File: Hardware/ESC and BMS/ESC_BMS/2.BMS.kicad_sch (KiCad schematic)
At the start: 0 parts

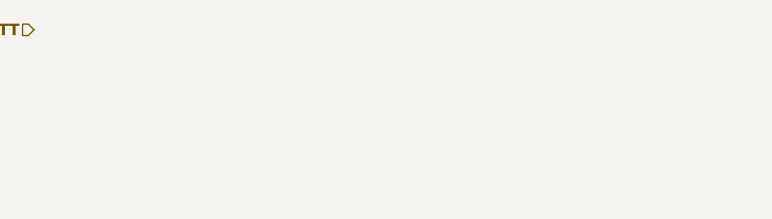
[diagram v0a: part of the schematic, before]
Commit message: Updated 2.BMS.kicad_sch to add bulk capacitance
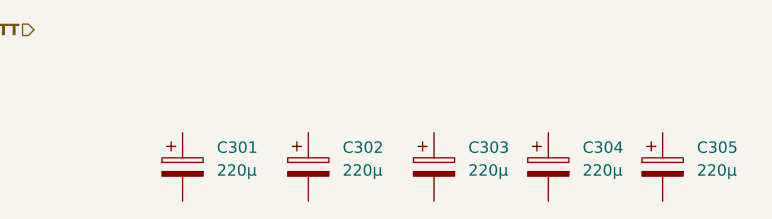
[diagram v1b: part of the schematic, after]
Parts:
- added C301, C302, C303, C304, C305: 220µ, Capacitor_SMD:CP_Elec_6.3x5.9, symbol Device:C_Polarized

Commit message: initial BMS work
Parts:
- added U12: BQ2969T, symbol ESC_BMS:BQ2969T
- renumbered C301 to C21, C302 to C22, C303 to C23, C304 to C24, C305 to C25
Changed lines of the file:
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@@
 		(dnp no)
 		(fields_autoplaced yes)
-		(property "Reference" "C301"
+		(property "Reference" "C21"
 			(at 48.26 35.9409 0)
 			(effects
@@
 			(project ""
 				(path "/64aee9f2-a448-43ef-b28d-f00e276bd9f5/eb2740b7-11f5-4644-9e72-e71a449b99af"
-					(reference "C301")
+					(reference "C21")
+					(unit 1)
+				)
+			)
+		)
+	)
+	(symbol
+		(lib_id "ESC_BMS:BQ2969T")
+		(at 95.25 54.61 0)
+		(unit 1)
+		(exclude_from_sim no)
+		(in_bom yes)
+		(on_board yes)
+		(dnp no)
+		(fields_autoplaced yes)
+		(property "Reference" "U12"
+			(at 97.79 46.99 0)
+			(effects
+				(font
+					(size 1.27 1.27)
+				)
+			)
+		)
+		(property "Value" "BQ2969T"
+			(at 97.79 49.53 0)
+			(effects
+				(font
+					(size 1.27 1.27)
+				)
+			)
+		)
+		(property "Footprint" ""
+			(at 95.25 54.61 0)
+			(effects
+				(font
+					(size 1.27 1.27)
+				)
+				(hide yes)
+			)
+		)
+		(property "Datasheet" "https://www.ti.com/lit/ds/symlink/bq2962.pdf?ts=1761657217789&ref_url=https%253A%252F%252Fwww.ti.com%252Fproduct%252FBQ2962"
+			(at 97.282 72.644 0)
+			(effects
+				(font
+					(size 1.27 1.27)
+				)
+				(hide yes)
+			)
+		)
+		(property "Description" "BQ296xxx Overvoltage Protection for 2-Series, 3-Series, and 4-Series Cell Li-Ion Batteries with Regulated Output Supply"
+			(at 98.298 76.2 0)
+			(effects
+				(font
+					(size 1.27 1.27)
+				)
+				(hide yes)
+			)
+		)
+		(pin "3"
+		)
+		(pin "4"
+		)
+		(pin "2"
+		)
+		(pin "9"
+		)
+		(pin "8"
+		)
+		(pin "7"
+		)
+		(pin "6"
+		)
+		(pin "1"
+		)
+		(pin "5"
+		)
+		(instances
+			(project ""
+				(path "/64aee9f2-a448-43ef-b28d-f00e276bd9f5/eb2740b7-11f5-4644-9e72-e71a449b99af"
+					(reference "U12")
 					(unit 1)
 				)
@@
 		(dnp no)
 		(fields_autoplaced yes)
-		(property "Reference" "C305"
+		(property "Reference" "C25"
 			(at 101.6 35.9409 0)
 			(effects
@@
 			(project "SPROJ3EE_ESC_BMS"
 				(path "/64aee9f2-a448-43ef-b28d-f00e276bd9f5/eb2740b7-11f5-4644-9e72-e71a449b99af"
-					(reference "C305")
+					(reference "C25")
 					(unit 1)
 				)
@@
 		(dnp no)
 		(fields_autoplaced yes)
-		(property "Reference" "C303"
+		(property "Reference" "C23"
 			(at 76.2 35.9409 0)
 			(effects
@@
 			(project "SPROJ3EE_ESC_BMS"
 				(path "/64aee9f2-a448-43ef-b28d-f00e276bd9f5/eb2740b7-11f5-4644-9e72-e71a449b99af"
-					(reference "C303")
+					(reference "C23")
 					(unit 1)
 				)
@@
 		(dnp no)
 		(fields_autoplaced yes)
-		(property "Reference" "C304"
+		(property "Reference" "C24"
 			(at 88.9 35.9409 0)
 			(effects
@@
 			(project "SPROJ3EE_ESC_BMS"
 				(path "/64aee9f2-a448-43ef-b28d-f00e276bd9f5/eb2740b7-11f5-4644-9e72-e71a449b99af"
-					(reference "C304")
+					(reference "C24")
 					(unit 1)
 				)
@@
 		(dnp no)
 		(fields_autoplaced yes)
-		(property "Reference" "C302"
+		(property "Reference" "C22"
 			(at 62.23 35.9409 0)
 			(effects
@@
 			(project "SPROJ3EE_ESC_BMS"
 				(path "/64aee9f2-a448-43ef-b28d-f00e276bd9f5/eb2740b7-11f5-4644-9e72-e71a449b99af"
-					(reference "C302")
-					(unit 1)
-				)
+					(reference "C22")
+					(unit 1)
+				)

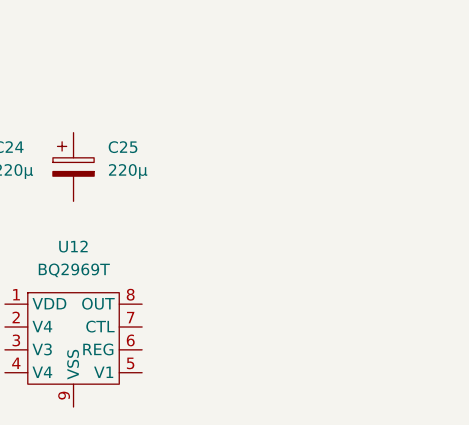
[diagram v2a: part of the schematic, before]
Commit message: some more BMS work + fixed RP2040 XIN/XOUT shortage
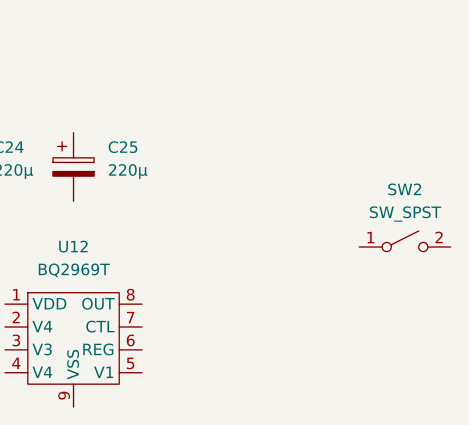
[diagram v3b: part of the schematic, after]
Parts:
- added SW2: SW_SPST, symbol Switch:SW_SPST
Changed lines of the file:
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@@
+	)
+	(symbol
+		(lib_id "Switch:SW_SPST")
+		(at 134.62 46.99 0)
+		(unit 1)
+		(exclude_from_sim no)
+		(in_bom yes)
+		(on_board yes)
+		(dnp no)
+		(fields_autoplaced yes)
+		(property "Reference" "SW2"
+			(at 134.62 40.64 0)
+			(effects
+				(font
+					(size 1.27 1.27)
+				)
+			)
+		)
+		(property "Value" "SW_SPST"
+			(at 134.62 43.18 0)
+			(effects
+				(font
+					(size 1.27 1.27)
+				)
+			)
+		)
+		(property "Footprint" ""
+			(at 134.62 46.99 0)
+			(effects
+				(font
+					(size 1.27 1.27)
+				)
+				(hide yes)
+			)
+		)
+		(property "Datasheet" "~"
+			(at 134.62 46.99 0)
+			(effects
+				(font
+					(size 1.27 1.27)
+				)
+				(hide yes)
+			)
+		)
+		(property "Description" "Single Pole Single Throw (SPST) switch"
+			(at 134.62 46.99 0)
+			(effects
+				(font
+					(size 1.27 1.27)
+				)
+				(hide yes)
+			)
+		)
+		(pin "1"
+		)
+		(pin "2"
+		)
+		(instances
+			(project ""
+				(path "/64aee9f2-a448-43ef-b28d-f00e276bd9f5/eb2740b7-11f5-4644-9e72-e71a449b99af"
+					(reference "SW2")
+					(unit 1)
+				)
+			)
+		)
 	)
 	(symbol

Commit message: BMS almost full
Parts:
- added C26, C27, C28, C29, C35, C38: 100n, Capacitor_SMD:C_0603_1608Metric, symbol Device:C
- added C30, C36: 100n, Capacitor_SMD:C_0805_2012Metric_Pad1.18x1.45mm_HandSolder, symbol Device:C
- added C31: 47nF, symbol Device:C_Polarized
- added C32, C33: 1uf, symbol Device:C_Polarized
- added C34: 47uF, symbol Device:C
- added D5, D6: BZX79, Diode_THT:D_DO-35_SOD27_P10.16mm_Horizontal, symbol Diode:ZPDxx
- added D7, D8: LED, symbol Device:LED
- added D9: LED_Dual, symbol Device:LED_Dual_AAKK
- added Q10, Q8: NTD25P03LT4G, symbol Simulation_SPICE:PMOS
- added Q9: NMOS, symbol Simulation_SPICE:NMOS
- added R13, R14: 100k, symbol Device:R
- added R15: 143k, symbol Device:R
- added R16: 1M, symbol Device:R
- added R17: 100, symbol Device:R
- added R18: 0.2, symbol Device:R
- added R19, R20, R21, R22, R24, R25: 1k, symbol Device:R
- added R23: 511, symbol Device:R
- added R26, R27: ?, symbol Device:R
- added TH2: ?, symbol Device:Thermistor_NTC
- added U13: 74AUC2G08, Package_SO:SSOP-8_2.95x2.8mm_P0.65mm, symbol 74xGxx:74AUC2G08
- added U14: TPS25926, Package_SON:VSON-10-1EP_3x3mm_P0.5mm_EP1.65x2.4mm_ThermalVias, symbol Power_Management:TPS2592xx
- added U16: BQ2057, symbol ESC_BMS:BQ2057
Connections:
- net +VBATT: now also SW2.1 (A)
- net VDD: now reaches U12.1 (VDD)
- net VDD: now also C30.1, R17.2
- net at U12.3 (V3): now also C28.1, R19.1
- net at U12.4 (V2): now also C28.2, C29.1, R20.1
- net at U12.5 (V1): now also C29.2, R21.1
- net at U12.6 (REG): now also C34.1
- net at U12.8 (OUT): now also Q9.2 (G)
- net GND: now reaches U12.9 (VSS)
- net GND: now also C26.2, C27.2, C30.2, C31.2, C32.2, C33.2, C34.2, C35.2, C36.1, C36.2, C38.2, D6.1 (K), Q9.3 (S), R14.2, R15.2, R18.1, R22.1, R24.1, R25.1, R26.2, R27.1, TH2.1, U13.4 (GND), U14.11 (GND), U16.3 (VCC), U16.6 (VSS), U16.8 (COMP)
- net at SW2.2 (B): now also Q8.3 (S)
- new net: C32.1, D5.2 (A), Q8.1 (D), R13.2, R16.1, U14.3 (VIN), U14.4 (VIN), U14.5 (VIN)
- new net: C31.1, U14.1 (dV/dT)
- new net: R26.1, R27.2, TH2.2, U16.4 (TS)
- new net: D9.4 (K2), R22.2
- new net: R15.1, U14.10 (ILIM)
- new net: R16.2, U14.2 (EN/UVLO)
- new net: C33.1, Q9.1 (D), R17.1, R19.2, U14.6 (OUT), U14.7 (OUT), U14.8 (OUT)
- new net: D9.2 (A2), D9.3 (K1), R24.2, U16.5 (STAT)
- new net: C38.1, Q10.1 (D), U16.2 (BAT)
- new net: Q10.3 (S), R18.2, U16.1 (SNS)
- new net: D5.1 (K), R14.1
- new net: D9.1 (A1), R23.2
- new net: Q10.2 (G), R25.2, U16.7 (CC)
- new net: D6.2 (A), R23.1
- new net: Q8.2 (G), R13.1
- new net: C35.1, R21.2
- new net VMID: R20.2
- no-connect marks 0 -> 1
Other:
- note added: "BQ2057"
- note added: "BQ2969T"
- note added: "Balancing"
- note added: "Charging"
- note added: "Decoupling caps"
- note added: "FOR Itrip 5A"
- note added: "OCP"
- note added: "RPP"
- note added: "TPS25926"
- moved on the sheet: C21, C22, C23, C24, C25, SW2

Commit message: more BMS
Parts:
- removed C26, C28, C35: 100n, Capacitor_SMD:C_0603_1608Metric, symbol Device:C
- removed C31: 47nF, symbol Device:C_Polarized
- removed C32, C33: 1uf, symbol Device:C_Polarized
- removed D9: LED_Dual, symbol Device:LED_Dual_AAKK
- removed R13: 100k, symbol Device:R
- removed R15: 143k, symbol Device:R
- removed R21: 1k, symbol Device:R
- removed R26, R27: ?, symbol Device:R
- removed TH2: ?, symbol Device:Thermistor_NTC
- removed U13: 74AUC2G08, Package_SO:SSOP-8_2.95x2.8mm_P0.65mm, symbol 74xGxx:74AUC2G08
- removed U14: TPS25926, Package_SON:VSON-10-1EP_3x3mm_P0.5mm_EP1.65x2.4mm_ThermalVias, symbol Power_Management:TPS2592xx
- added C29: 100n, Capacitor_SMD:C_0603_1608Metric, symbol Device:C
- added F2: RUEF Polyfuse, Resistor_THT:R_Axial_DIN0207_L6.3mm_D2.5mm_P10.16mm_Horizontal, symbol Device:Polyfuse
- added Q11: SQJ141ELP, symbol Simulation_SPICE:PMOS
- added R14: 10k, symbol Device:R
- added R25: 1M, symbol Device:R
- C34: value 47uF -> 470nF
- D7: value LED -> KG EELP41.22
- D8: value LED -> LR Q976.01
- Q8: value NTD25P03LT4G -> SQJ141ELP
- R13: renamed from R14; value 100k -> 27k
- R15: renamed from R18; value 0.2 -> ?
- R16: value 1M -> 10k
- renumbered C27 to C21, C30 to C22, C36 to C23, C21 to C24, C22 to C25, C23 to C26, C24 to C27, C25 to C28, C29 to C31, C38 to C32, Q9 to Q10, Q10 to Q9, R23 to R17, R25 to R18, R24 to R19, R19 to R20, R22 to R21, R20 to R22, R17 to R23, U16 to U12, U12 to U13
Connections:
- net GND: now also C24.2, C25.2, C26.2, C27.2, C28.2, R16.1, C29.2, R14.2
- net +VPROT: now reaches C24.1
- net +VPROT: now also C25.1, C26.1, C27.1, C28.1, C32.1, Q9.1 (D), U12.2 (BAT), Q11.3 (S)
- net at U12.4 (TS): now also R16.2, R14.1
- net at R21.2: now also D7.1 (K)
- net at R20.2, R23.1: now also F2.2, Q11.1 (D), R25.1; no longer Q10.1 (D)
- net at Q8.3 (S): now also D5.1 (K), C29.1, F2.1; no longer SW2.2 (B)
- net at D8.1 (K): now also D7.2 (A), R19.2, U12.5 (STAT)
- net at D8.2 (A): now also R17.2
- net VIN: now reaches C21.1
- net at U13.3 (V3): now also C31.2, U13.4 (V2), U13.5 (V1); no longer R20.1
- net at C31.1, R22.1: no longer U13.4 (V2)
- net at R13.1: now also D5.2 (A), Q8.2 (G); no longer D5.1 (K)
- net DC: now reaches D6.2 (A), R17.1
- net at U13.2 (V4): now also R20.1
- net at U13.7 (CTL): now also R25.2
- new net: Q10.1 (D), Q11.2 (G)
- new net: Q8.1 (D), SW2.2 (B)
- no-connect marks 1 -> 0
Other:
- note removed: "Decoupling caps"
- note removed: "FOR Itrip 5A"
- moved on the sheet: C21, C22, C23, C24, C25, C26, C27, C28, C31, C32, C34, D5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

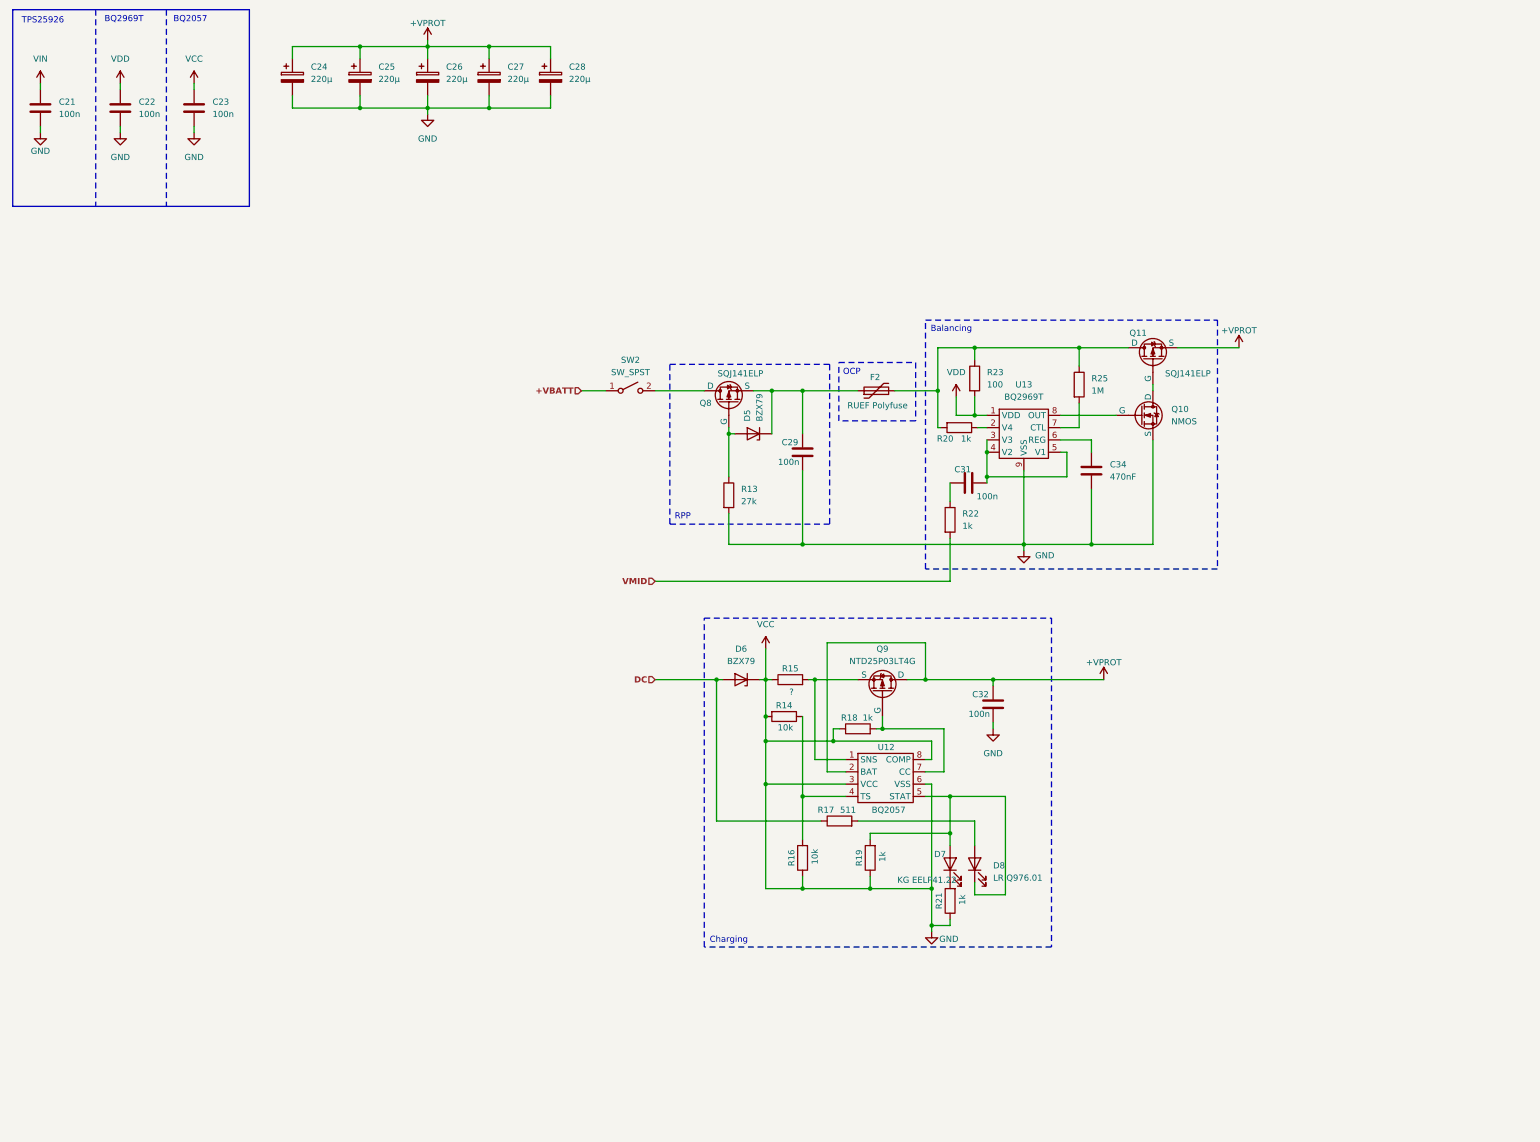
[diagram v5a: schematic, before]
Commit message: Simulations for BMS start and footprints
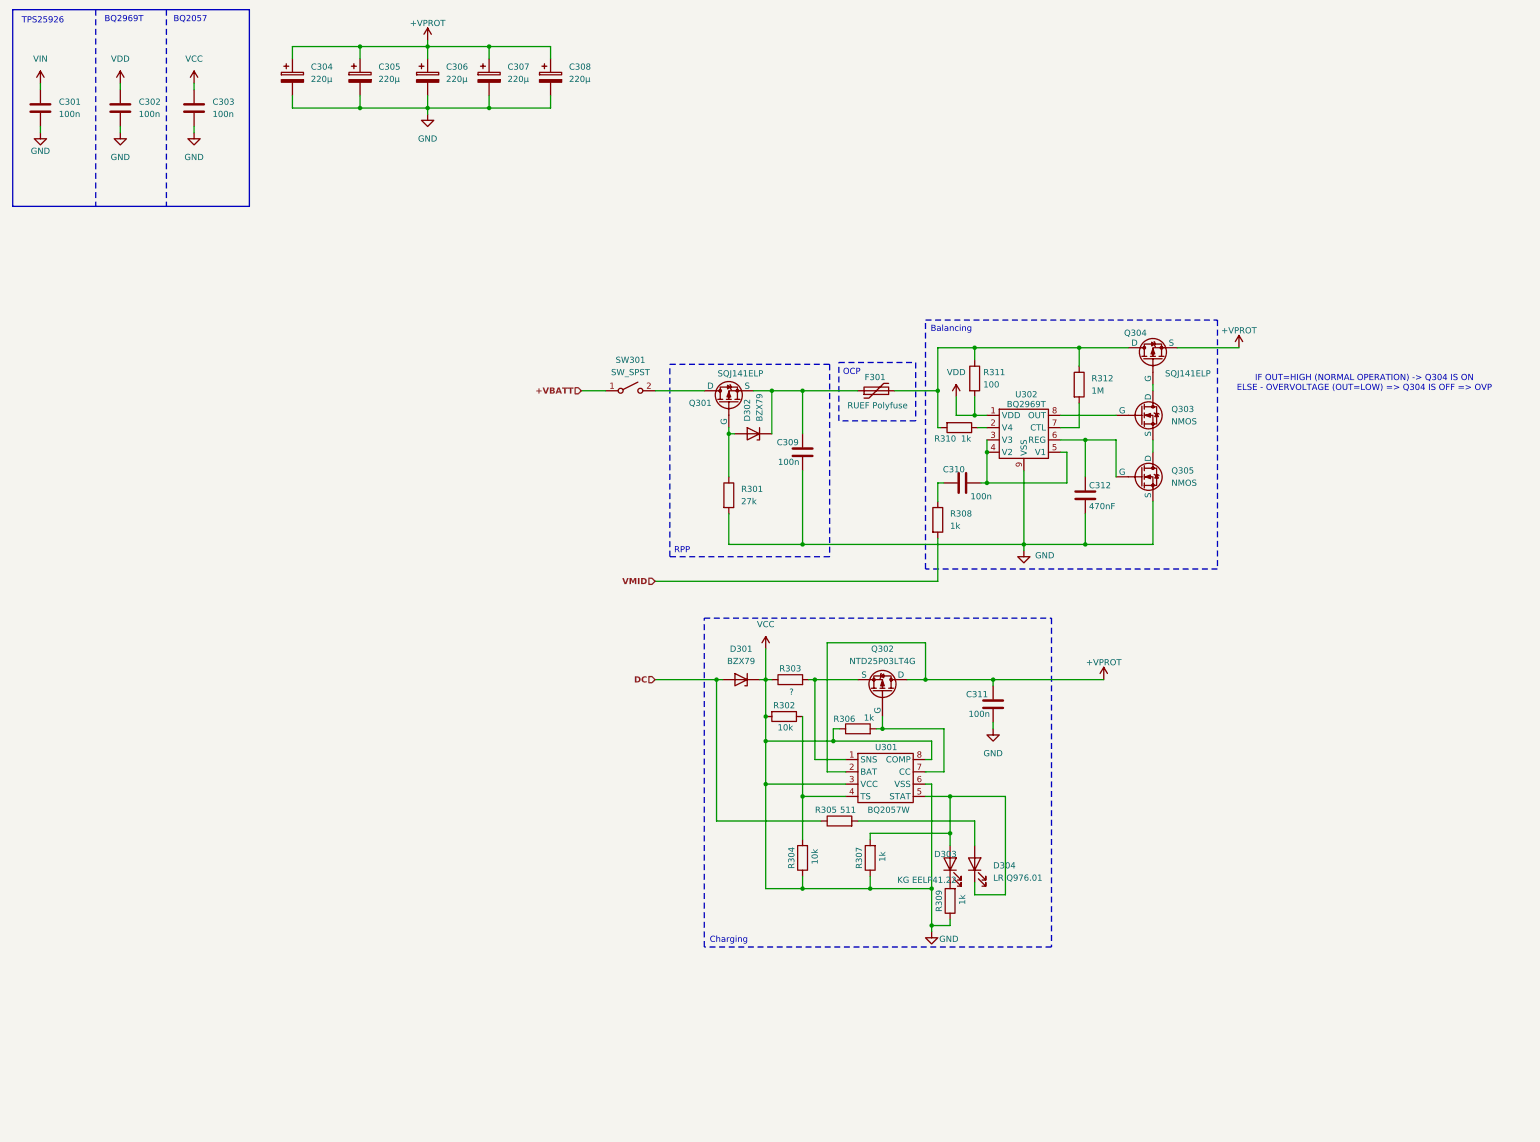
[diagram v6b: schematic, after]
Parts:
- added Q305: NMOS, symbol Simulation_SPICE:NMOS
- U301: renamed from U12; value BQ2057 -> BQ2057W; footprint (none) -> Package_SO:SOIC-8_5.3x5.3mm_P1.27mm
- renumbered C21 to C301, C22 to C302, C23 to C303, C24 to C304, C25 to C305, C26 to C306, C27 to C307, C28 to C308, C29 to C309, C31 to C310, C32 to C311, C34 to C312, D6 to D301, D5 to D302, D7 to D303, D8 to D304, F2 to F301, Q8 to Q301, Q9 to Q302, Q10 to Q303, Q11 to Q304, R13 to R301, R14 to R302, R15 to R303, R16 to R304, R17 to R305, R18 to R306, R19 to R307, R22 to R308, R21 to R309, R20 to R310, R23 to R311, R25 to R312, SW2 to SW301, U13 to U302
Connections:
- net GND: now also Q305.3 (S); no longer Q303.3 (S)
- net at C312.1, U302.6 (REG): now also Q305.2 (G)
- new net: Q303.3 (S), Q305.1 (D)
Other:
- note added: "IF OUT=HIGH (NORMAL OPERATION) -> Q304 IS ON ELSE - OVERVOLTAGE (OUT=LOW) => Q304 IS OFF => OVP"
- moved on the sheet: C310, C312, R308

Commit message: Footprints + final schematic _/\_
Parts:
- removed C311: 100n, Capacitor_SMD:C_0603_1608Metric, symbol Device:C
- removed Q303: NMOS, symbol Simulation_SPICE:NMOS
- added Q303: SQJ141ELP, symbol Simulation_SPICE:PMOS
- renumbered C312 to C311, Q305 to Q304, Q304 to Q305
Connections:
- net VIN is gone; now on net +VPROT: C301.1
- net GND: now also Q304.1 (D); no longer Q304.3 (S)
- net at Q305.2 (G): now also Q303.1 (D)
- net at U302.8 (OUT): now also Q303.2 (G)
- new net: Q303.3 (S), Q304.3 (S)
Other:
- note added: "IF OUT=LOW (NORMAL OPERATION) -> Q305 IS ON ELSE - OVERVOLTAGE (OUT=HIGH) => Q305 IS OFF => OVP"
- note added: "IF REG=HIGH (NORMAL OPERATION) -> Q305 IS ON ELSE - UNDERVOLTAGE (REG=LOW) => Q305 IS OFF => UVP"
- note added: "VPROT"
- note removed: "IF OUT=HIGH (NORMAL OPERATION) -> Q304 IS ON ELSE - OVERVOLTAGE (OUT=LOW) => Q304 IS OFF => OVP"
- note removed: "TPS25926"
- moved on the sheet: C304, C305, C306, C307, C308, C311, D303, D304, Q302
